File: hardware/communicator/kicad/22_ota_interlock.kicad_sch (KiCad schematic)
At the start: 8 parts, among them J31 RUN link / REMOVE FOR OTA, U52 SN74LVC1G11DCKR, U53 SN74LVC1G11DCKR

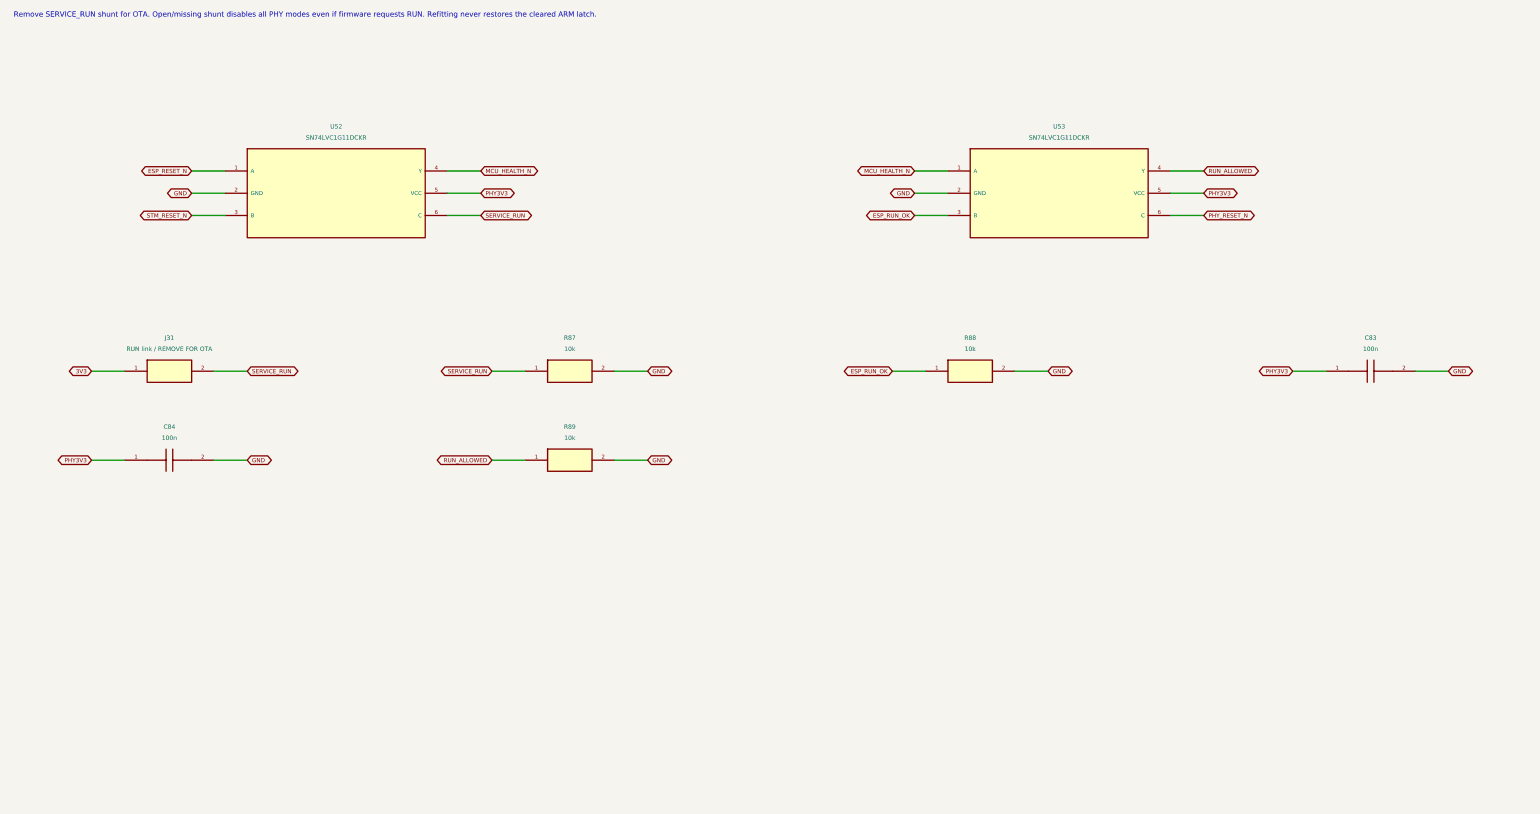
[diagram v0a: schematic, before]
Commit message: Fix OTA service interlock and durable activation policy
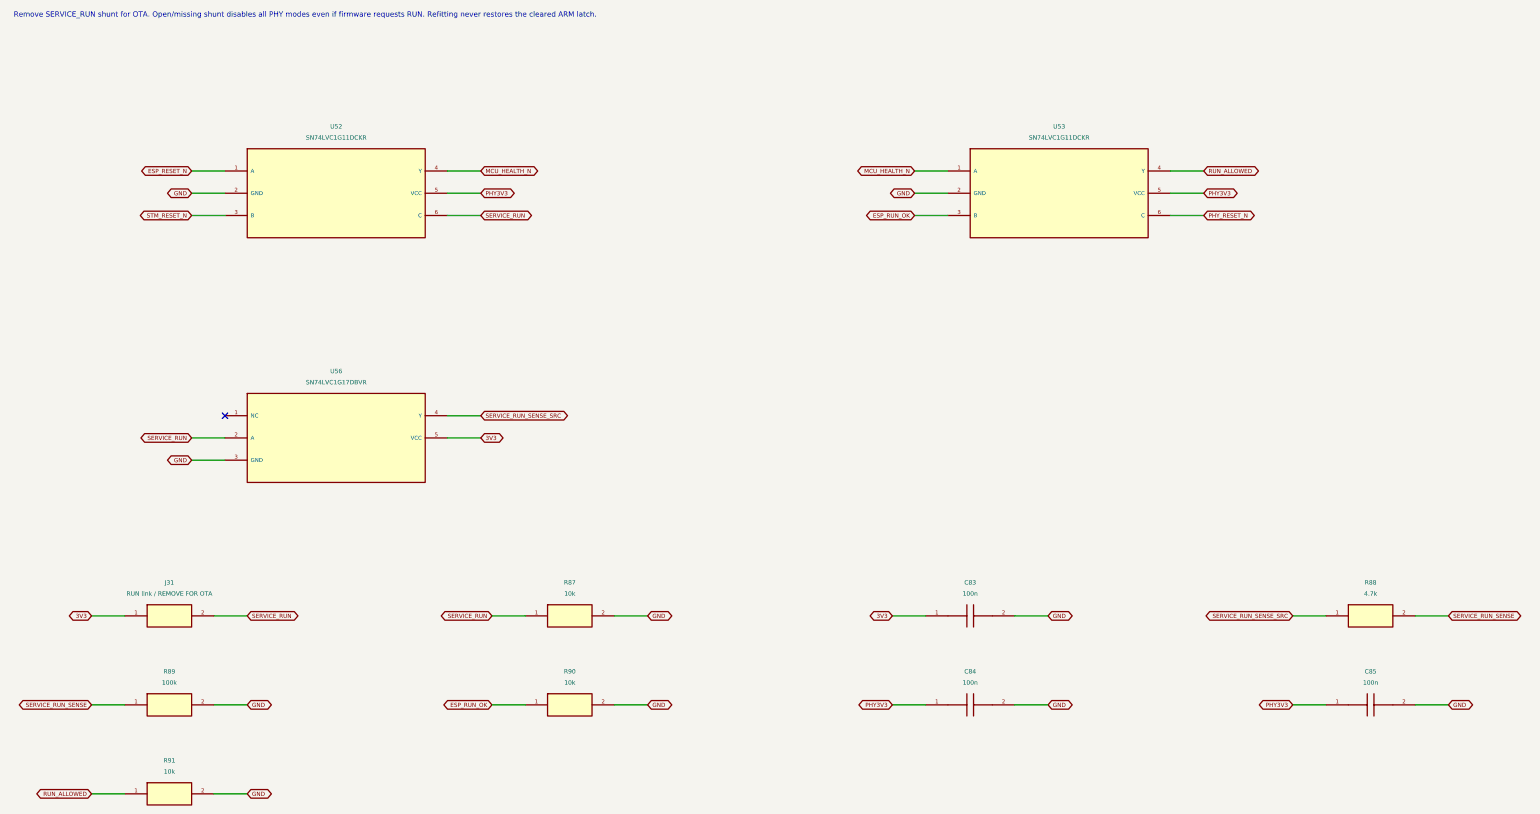
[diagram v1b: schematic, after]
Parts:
- added C85: 100n, CANView:Capacitor_SMD__C_0402_1005Metric, symbol CANView:CANView_communicator_C85
- added R90: 10k, CANView:Resistor_SMD__R_0402_1005Metric, symbol CANView:CANView_communicator_R90
- added R91: 10k, CANView:Resistor_SMD__R_0402_1005Metric, symbol CANView:CANView_communicator_R91
- added U56: SN74LVC1G17DBVR, CANView:Package_TO_SOT_SMD__SOT-23-5, symbol CANView:CANView_communicator_U56
- R88: value 10k -> 4.7k; MPN GEN-R-0402-10k-1% -> GEN-R-0402-4.7k-1%
- R89: value 10k -> 100k; MPN GEN-R-0402-10k-1% -> GEN-R-0402-100k-1%
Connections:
- net 3V3: now also C83.1, U56.5 (VCC)
- net ESP_RUN_OK: now also R90.1; no longer R88.1
- net GND: now also C85.2, R90.2, R91.2, U56.3 (GND); no longer R88.2
- net PHY3V3: now also C85.1; no longer C83.1
- net RUN_ALLOWED: now also R91.1; no longer R89.1
- net SERVICE_RUN: now also U56.2 (A)
- new net SERVICE_RUN_SENSE: R88.2, R89.1
- new net SERVICE_RUN_SENSE_SRC: R88.1, U56.4 (Y)
- no-connect marks 0 -> 1
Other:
- moved on the sheet: C83, C84, J31, R87, R88, R89
